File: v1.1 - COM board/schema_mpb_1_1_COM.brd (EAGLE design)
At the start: 100 x 80 mm, 2 parts, among them IC1 E73_2G4M04S, U1 ESP-WROOM-32

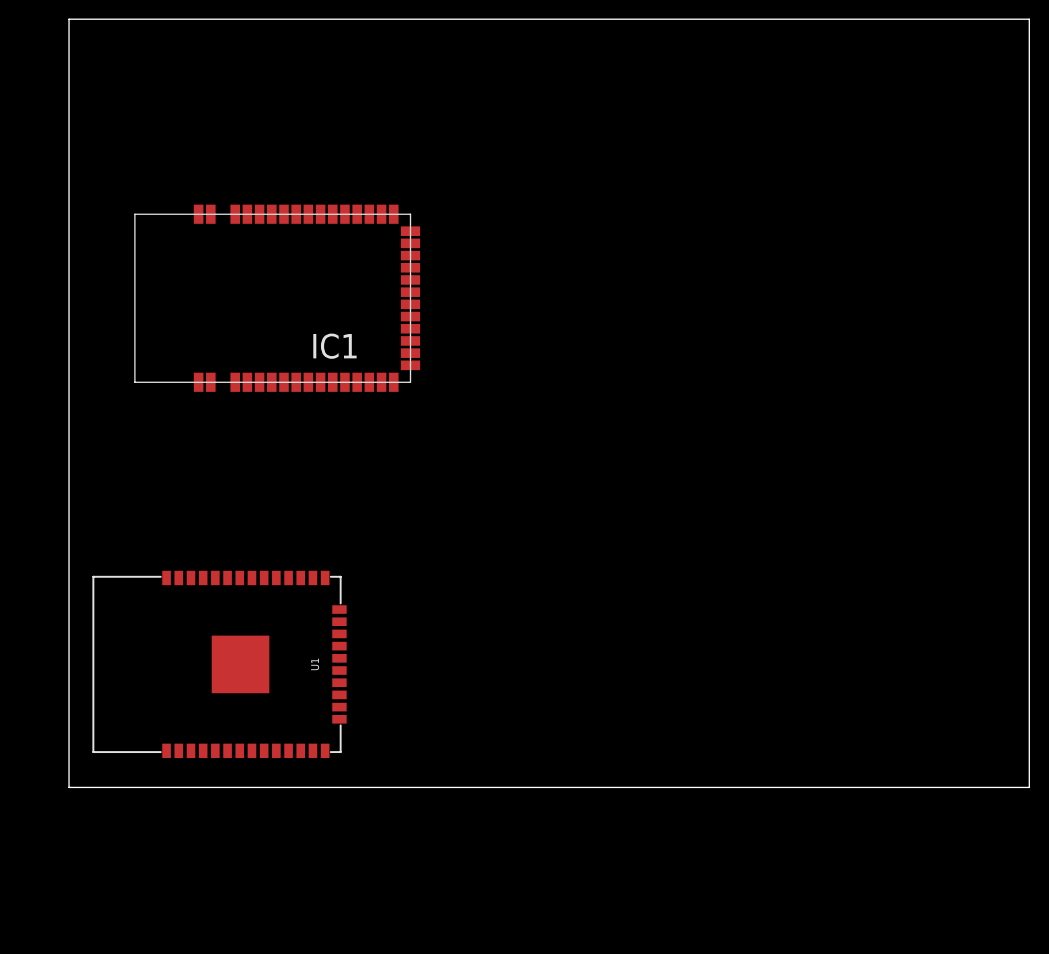
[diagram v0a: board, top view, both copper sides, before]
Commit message: Main board revisions
- Rerouted long tracks to other layers
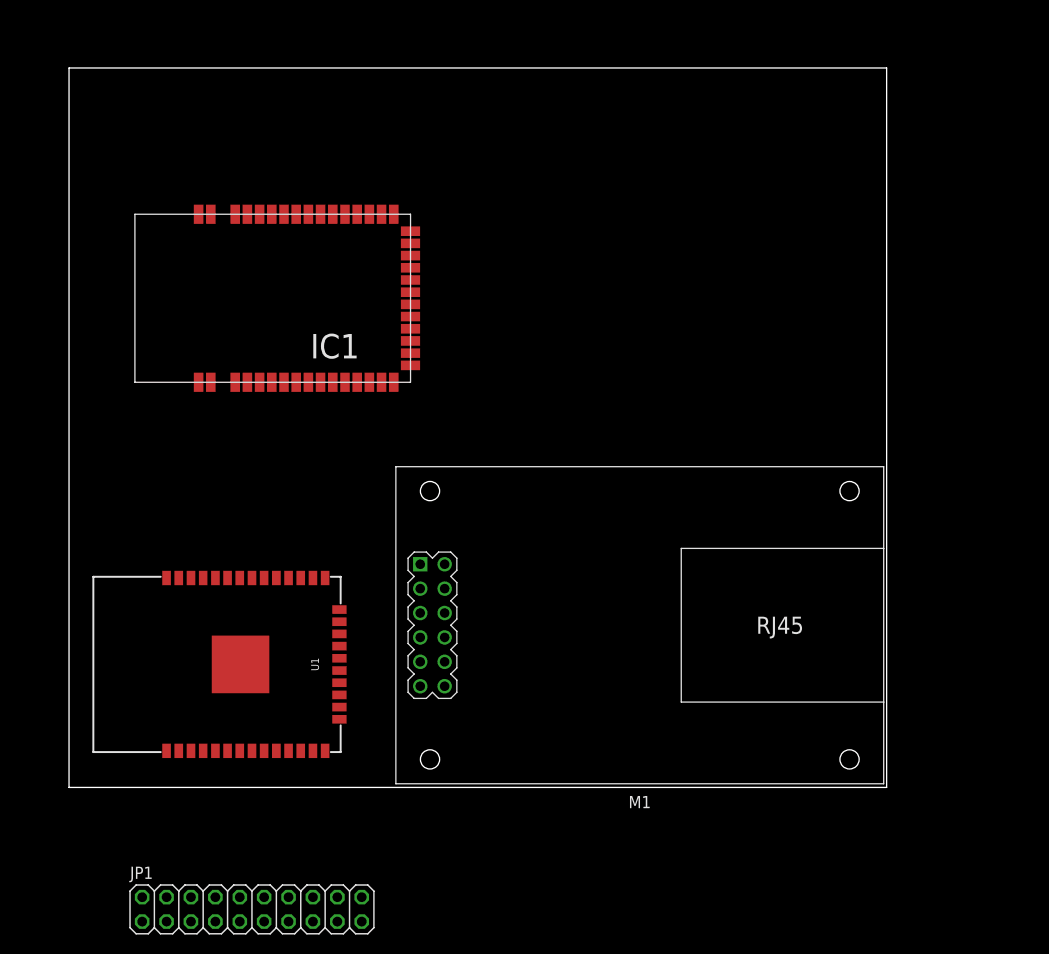
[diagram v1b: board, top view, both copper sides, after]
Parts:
- added JP1: (no value), pinhead:2X10
- added M1: ETHERNET-ENC28J60, diy-modules:ETHERNET-ENC28J60
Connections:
- new net 3V3: M1.2
- new net 5V: M1.12
- new net GND.1: M1.1
- new net GND.2: M1.11
- new net N$1: JP1.1
- new net N$10: JP1.19
- new net N$11: JP1.20
- new net N$12: JP1.18
- new net N$13: JP1.16
- new net N$14: JP1.14
- new net N$15: JP1.12
- new net N$16: JP1.10
- new net N$17: JP1.8
- new net N$18: JP1.6
- new net N$19: JP1.4
- new net N$2: JP1.3
- new net N$20: JP1.2
- new net N$3: JP1.5
- new net N$4: JP1.7
- new net N$5: JP1.9
- new net N$6: JP1.11
- new net N$7: JP1.13
- new net N$8: JP1.15
- new net N$9: JP1.17
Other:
- board size 100 x 80 mm -> 85.1 x 74.9 mm
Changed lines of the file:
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@@
 <setting verticaltext="up"/>
 </settings>
-<grid distance="50" unitdist="mil" unit="mil" style="lines" multiple="1" display="no" altdistance="5" altunitdist="mil" altunit="mil"/>
+<grid distance="50" unitdist="mil" unit="mil" style="lines" multiple="1" display="yes" altdistance="5" altunitdist="mil" altunit="mil"/>
 <layers>
 <layer number="1" name="Top" color="4" fill="1" visible="yes" active="yes"/>
@@
 <board>
 <plain>
-<wire x1="0" y1="0" x2="100" y2="0" width="0" layer="20"/>
-<wire x1="100" y1="0" x2="100" y2="80" width="0" layer="20"/>
-<wire x1="100" y1="80" x2="0" y2="80" width="0" layer="20"/>
-<wire x1="0" y1="80" x2="0" y2="0" width="0" layer="20"/>
+<wire x1="0" y1="0" x2="85.141" y2="0" width="0" layer="20"/>
+<wire x1="85.141" y1="0" x2="85.141" y2="74.92" width="0" layer="20"/>
+<wire x1="85.141" y1="74.92" x2="0" y2="74.92" width="0" layer="20"/>
+<wire x1="0" y1="74.92" x2="0" y2="0" width="0" layer="20"/>
 </plain>
 <attributes>
@@
 <element name="IC1" library="E73-2G4M04S" package="E73_2G4M04S" value="E73_2G4M04S" x="35.56" y="59.69" rot="R180"/>
 <element name="U1" library="esp32" package="ESP-WROOM-32" value="ESP-WROOM-32" x="17.86" y="12.81" rot="R180"/>
+<element name="M1" library="diy-modules" package="ETHERNET-ENC28J60" value="ETHERNET-ENC28J60" x="59.436" y="16.891" rot="R180"/>
+<element name="JP1" library="pinhead" library_urn="urn:adsk.eagle:library:325" package="2X10" package3d_urn="urn:adsk.eagle:package:22405/2" value="" x="19.05" y="-12.7"/>
 </elements>
 <signals>
@@
 </signal>
 <signal name="3V3">
+<contactref element="M1" pad="2"/>
+</signal>
+<signal name="GND.1">
+<contactref element="M1" pad="1"/>
+</signal>
+<signal name="GND.2">
+<contactref element="M1" pad="11"/>
+</signal>
+<signal name="5V">
+<contactref element="M1" pad="12"/>
+</signal>
+<signal name="N$1">
+<contactref element="JP1" pad="1"/>
+</signal>
+<signal name="N$2">
+<contactref element="JP1" pad="3"/>
+</signal>
+<signal name="N$3">
+<contactref element="JP1" pad="5"/>
+</signal>
+<signal name="N$4">
+<contactref element="JP1" pad="7"/>
+</signal>
+<signal name="N$5">
+<contactref element="JP1" pad="9"/>
+</signal>
+<signal name="N$6">
+<contactref element="JP1" pad="11"/>
+</signal>
+<signal name="N$7">
+<contactref element="JP1" pad="13"/>
+</signal>
+<signal name="N$8">
+<contactref element="JP1" pad="15"/>
+</signal>
+<signal name="N$9">
+<contactref element="JP1" pad="17"/>
+</signal>
+<signal name="N$10">
+<contactref element="JP1" pad="19"/>
+</signal>
+<signal name="N$11">
+<contactref element="JP1" pad="20"/>
+</signal>
+<signal name="N$12">
+<contactref element="JP1" pad="18"/>
+</signal>
+<signal name="N$13">
+<contactref element="JP1" pad="16"/>
+</signal>
+<signal name="N$14">
+<contactref element="JP1" pad="14"/>
+</signal>
+<signal name="N$15">
+<contactref element="JP1" pad="12"/>
+</signal>
+<signal name="N$16">
+<contactref element="JP1" pad="10"/>
+</signal>
+<signal name="N$17">
+<contactref element="JP1" pad="8"/>
+</signal>
+<signal name="N$18">
+<contactref element="JP1" pad="6"/>
+</signal>
+<signal name="N$19">
+<contactref element="JP1" pad="4"/>
+</signal>
+<signal name="N$20">
+<contactref element="JP1" pad="2"/>
 </signal>
 </signals>
 </board>
 </drawing>
+<compatibility>
+<note version="8.2" severity="warning">
+Since Version 8.2, EAGLE supports online libraries. The ids
+of those online libraries will not be understood (or retained)
+with this version.
+</note>
+<note version="8.3" severity="warning">
+Since Version 8.3, EAGLE supports URNs for individual library
+assets (packages, symbols, and devices). The URNs of those assets
+will not be understood (or retained) with this version.
+</note>
+<note version="8.3" severity="warning">
+Since Version 8.3, EAGLE supports the association of 3D packages
+with devices in libraries, schematics, and board files. Those 3D
+packages will not be understood (or retained) with this version.
+</note>
+</compatibility>
 </eagle>

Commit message: Main board
- Tidied tracks
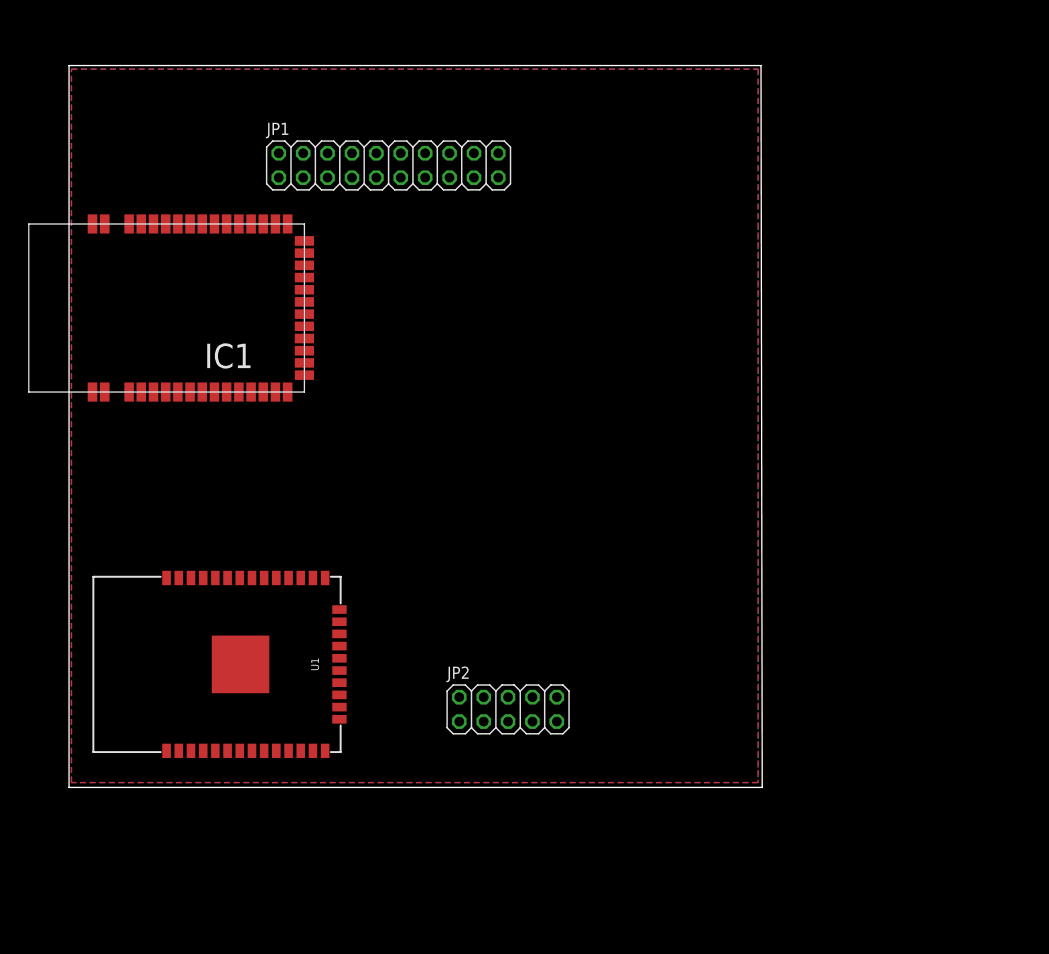
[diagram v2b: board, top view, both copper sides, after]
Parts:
- removed M1: ETHERNET-ENC28J60, diy-modules:ETHERNET-ENC28J60
- added JP2: (no value), pinhead:2X05
- moved JP1 78.8 mm to (33.3, 64.8)
- moved IC1 11.1 mm to (24.5, 58.7)
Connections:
- net N$1 renamed ETH_SCK
- net N$14 renamed USB_OTG_HS_DM
- net N$15 renamed NRF_CS
- net N$16 renamed NRF_MISO
- net N$17 renamed NRF_SCK
- net N$18 renamed CAN1_TX
- net N$19 renamed ETH_MISO
- net N$2 renamed ETH_MOSI
- net N$20 renamed ETH_SS
- net N$3 renamed CAN1_RX
- net N$4 renamed NRF_MOSI
- net N$5 renamed NRF_CE
- net N$6 renamed NRF_IRQ
- net N$7 renamed USB_OTG_HS_DP
- removed net 3V3: M1.2
- removed net 5V: M1.12
- removed net GND.1: M1.1
- removed net GND.2: M1.11
- removed net N$11: JP1.20
- removed net N$12: JP1.18
- removed net N$13: JP1.16
- new net +3.3V: JP1.19, JP1.20
- new net +5V: JP1.15, JP1.16
- new net GND: JP1.17, JP1.18
- new net N$1: U1.1
- new net N$2: U1.2
- new net N$3: U1.35
- new net N$4: U1.34
- new net N$5: U1.15
- new net N$6: IC1.0, IC1.1, IC1.15, IC1.2, IC1.42, IC1.43
- new net N$7: IC1.38
- net N$10: now also IC1.36; no longer JP1.19
- net N$8: now also IC1.37; no longer JP1.15
- net N$9: now also IC1.16; no longer JP1.17
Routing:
- added copper zone on layer 16, net N$11
- added copper zone on layer 1, net N$14
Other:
- board size 85.1 x 74.9 mm -> 72.2 x 75.2 mm
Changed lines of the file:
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@@
 <setting verticaltext="up"/>
 </settings>
-<grid distance="50" unitdist="mil" unit="mil" style="lines" multiple="1" display="yes" altdistance="5" altunitdist="mil" altunit="mil"/>
+<grid distance="20" unitdist="mil" unit="mil" style="lines" multiple="1" display="yes" altdistance="5" altunitdist="mil" altunit="mil"/>
 <layers>
 <layer number="1" name="Top" color="4" fill="1" visible="yes" active="yes"/>
@@
 <board>
 <plain>
-<wire x1="0" y1="0" x2="85.141" y2="0" width="0" layer="20"/>
-<wire x1="85.141" y1="0" x2="85.141" y2="74.92" width="0" layer="20"/>
-<wire x1="85.141" y1="74.92" x2="0" y2="74.92" width="0" layer="20"/>
-<wire x1="0" y1="74.92" x2="0" y2="0" width="0" layer="20"/>
+<wire x1="0" y1="0" x2="72.187" y2="0" width="0" layer="20"/>
+<wire x1="72.187" y1="0" x2="72.06" y2="75.174" width="0" layer="20"/>
+<wire x1="72.06" y1="75.174" x2="0" y2="75.174" width="0" layer="20"/>
+<wire x1="0" y1="75.174" x2="0" y2="0" width="0" layer="20"/>
 </plain>
 <attributes>
@@
 </autorouter>
 <elements>
-<element name="IC1" library="E73-2G4M04S" package="E73_2G4M04S" value="E73_2G4M04S" x="35.56" y="59.69" rot="R180"/>
-<element name="U1" library="esp32" package="ESP-WROOM-32" value="ESP-WROOM-32" x="17.86" y="12.81" rot="R180"/>
-<element name="M1" library="diy-modules" package="ETHERNET-ENC28J60" value="ETHERNET-ENC28J60" x="59.436" y="16.891" rot="R180"/>
-<element name="JP1" library="pinhead" library_urn="urn:adsk.eagle:library:325" package="2X10" package3d_urn="urn:adsk.eagle:package:22405/2" value="" x="19.05" y="-12.7"/>
+<element name="IC1" library="E73-2G4M04S" package="E73_2G4M04S" value="E73_2G4M04S" x="24.511" y="58.674" smashed="yes" rot="R180">
+<attribute name="NAME" x="19.191" y="46.204" size="2.54" layer="25" rot="R180"/>
+<attribute name="VALUE" x="20.871" y="51.824" size="2.54" layer="27" rot="R180"/>
+</element>
+<element name="U1" library="esp32" package="ESP-WROOM-32" value="ESP-WROOM-32" x="17.86" y="12.81" smashed="yes" rot="R180">
+<attribute name="NAME" x="25.62" y="12.81" size="0.8128" layer="25" rot="R270" align="center"/>
+<attribute name="VALUE" x="24.35" y="12.81" size="0.8128" layer="27" rot="R270" align="center"/>
+</element>
+<element name="JP1" library="pinhead" library_urn="urn:adsk.eagle:library:325" package="2X10" package3d_urn="urn:adsk.eagle:package:22405/2" value="" x="33.274" y="64.77" smashed="yes">
+<attribute name="NAME" x="20.574" y="67.945" size="1.27" layer="25" ratio="10"/>
+<attribute name="VALUE" x="20.574" y="60.325" size="1.27" layer="27"/>
+</element>
+<element name="JP2" library="pinhead" library_urn="urn:adsk.eagle:library:325" package="2X05" package3d_urn="urn:adsk.eagle:package:22470/2" value="" x="45.72" y="8.128" smashed="yes">
+<attribute name="NAME" x="39.37" y="11.303" size="1.27" layer="25" ratio="10"/>
+<attribute name="VALUE" x="39.37" y="3.683" size="1.27" layer="27"/>
+</element>
 </elements>
 <signals>
@@
 <contactref element="IC1" pad="14"/>
 </signal>
-<signal name="3V3">
-<contactref element="M1" pad="2"/>
-</signal>
-<signal name="GND.1">
-<contactref element="M1" pad="1"/>
-</signal>
-<signal name="GND.2">
-<contactref element="M1" pad="11"/>
-</signal>
-<signal name="5V">
-<contactref element="M1" pad="12"/>
+<signal name="ETH_SCK">
+<contactref element="JP1" pad="1"/>
+</signal>
+<signal name="ETH_MOSI">
+<contactref element="JP1" pad="3"/>
+</signal>
+<signal name="CAN1_RX">
+<contactref element="JP1" pad="5"/>
+</signal>
+<signal name="NRF_MOSI">
+<contactref element="JP1" pad="7"/>
+</signal>
+<signal name="NRF_CE">
+<contactref element="JP1" pad="9"/>
+</signal>
+<signal name="NRF_IRQ">
+<contactref element="JP1" pad="11"/>
+</signal>
+<signal name="USB_OTG_HS_DP">
+<contactref element="JP1" pad="13"/>
+</signal>
+<signal name="+5V">
+<contactref element="JP1" pad="15"/>
+<contactref element="JP1" pad="16"/>
+<wire x1="39.624" y1="63.5" x2="39.624" y2="66.04" width="0" layer="19" extent="1-1"/>
+</signal>
+<signal name="GND">
+<contactref element="JP1" pad="17"/>
+<contactref element="JP1" pad="18"/>
+<wire x1="42.164" y1="63.5" x2="42.164" y2="66.04" width="0" layer="19" extent="1-1"/>
+</signal>
+<signal name="+3.3V">
+<contactref element="JP1" pad="19"/>
+<contactref element="JP1" pad="20"/>
+<wire x1="44.704" y1="63.5" x2="44.704" y2="66.04" width="0" layer="19" extent="1-1"/>
+</signal>
+<signal name="USB_OTG_HS_DM">
+<contactref element="JP1" pad="14"/>
+</signal>
+<signal name="NRF_CS">
+<contactref element="JP1" pad="12"/>
+</signal>
+<signal name="NRF_MISO">
+<contactref element="JP1" pad="10"/>
+</signal>
+<signal name="NRF_SCK">
+<contactref element="JP1" pad="8"/>
+</signal>
+<signal name="CAN1_TX">
+<contactref element="JP1" pad="6"/>
+</signal>
+<signal name="ETH_MISO">
+<contactref element="JP1" pad="4"/>
+</signal>
+<signal name="ETH_SS">
+<contactref element="JP1" pad="2"/>
 </signal>
 <signal name="N$1">
-<contactref element="JP1" pad="1"/>
+<contactref element="U1" pad="1"/>
 </signal>
 <signal name="N$2">
-<contactref element="JP1" pad="3"/>
+<contactref element="U1" pad="2"/>
 </signal>
 <signal name="N$3">
-<contactref element="JP1" pad="5"/>
+<contactref element="U1" pad="35"/>
 </signal>
 <signal name="N$4">
-<contactref element="JP1" pad="7"/>
+<contactref element="U1" pad="34"/>
 </signal>
 <signal name="N$5">
-<contactref element="JP1" pad="9"/>
+<contactref element="U1" pad="15"/>
 </signal>
 <signal name="N$6">
-<contactref element="JP1" pad="11"/>
+<contactref element="IC1" pad="0"/>
+<contactref element="IC1" pad="43"/>
+<contactref element="IC1" pad="1"/>
+<contactref element="IC1" pad="2"/>
+<contactref element="IC1" pad="15"/>
+<contactref element="IC1" pad="42"/>
+<wire x1="6.256" y1="41.174" x2="22.766" y2="41.174" width="0" layer="19" extent="1-1"/>
+<wire x1="3.716" y1="41.174" x2="6.256" y2="41.174" width="0" layer="19" extent="1-1"/>
+<wire x1="2.446" y1="41.174" x2="3.716" y2="41.174" width="0" layer="19" extent="1-1"/>
+<wire x1="2.446" y1="58.674" x2="2.446" y2="41.174" width="0" layer="19" extent="1-1"/>
+<wire x1="3.716" y1="58.674" x2="2.446" y2="58.674" width="0" layer="19" extent="1-1"/>
 </signal>
 <signal name="N$7">
-<contactref element="JP1" pad="13"/>
+<contactref element="IC1" pad="38"/>
 </signal>
 <signal name="N$8">
-<contactref element="JP1" pad="15"/>
+<contactref element="IC1" pad="37"/>
 </signal>
 <signal name="N$9">
-<contactref element="JP1" pad="17"/>
+<contactref element="IC1" pad="16"/>
+</signal>
+<signal name="N$14">
+<polygon width="0.1524" layer="1">
+<vertex x="0.254" y="74.803"/>
+<vertex x="71.755" y="74.803"/>
+<vertex x="71.755" y="0.508"/>
+<vertex x="0.254" y="0.508"/>
+</polygon>
 </signal>
 <signal name="N$10">
-<contactref element="JP1" pad="19"/>
+<contactref element="IC1" pad="36"/>
 </signal>
 <signal name="N$11">
-<contactref element="JP1" pad="20"/>
-</signal>
-<signal name="N$12">
-<contactref element="JP1" pad="18"/>
-</signal>
-<signal name="N$13">
-<contactref element="JP1" pad="16"/>
-</signal>
-<signal name="N$14">
-<contactref element="JP1" pad="14"/>
-</signal>
-<signal name="N$15">
-<contactref element="JP1" pad="12"/>
-</signal>
-<signal name="N$16">
-<contactref element="JP1" pad="10"/>
-</signal>
-<signal name="N$17">
-<contactref element="JP1" pad="8"/>
-</signal>
-<signal name="N$18">
-<contactref element="JP1" pad="6"/>
-</signal>
-<signal name="N$19">
-<contactref element="JP1" pad="4"/>
-</signal>
-<signal name="N$20">
-<contactref element="JP1" pad="2"/>
+<polygon width="0.1524" layer="16">
+<vertex x="0.254" y="74.803"/>
+<vertex x="71.755" y="74.803"/>
+<vertex x="71.755" y="58.674"/>
+<vertex x="71.755" y="0.508"/>
+<vertex x="0.254" y="0.508"/>
+</polygon>
 </signal>
 </signals>
